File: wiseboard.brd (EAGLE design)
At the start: 80 x 55 mm, 91 parts, among them IC1 MCP73871-2CCI/ML-ND, IC2 LM358MX, Q1 IRLML6402TRPBF, Q2 IRLML6402TRPBF, U1 LT1945EMSPBF, X1 1528-1438-ND

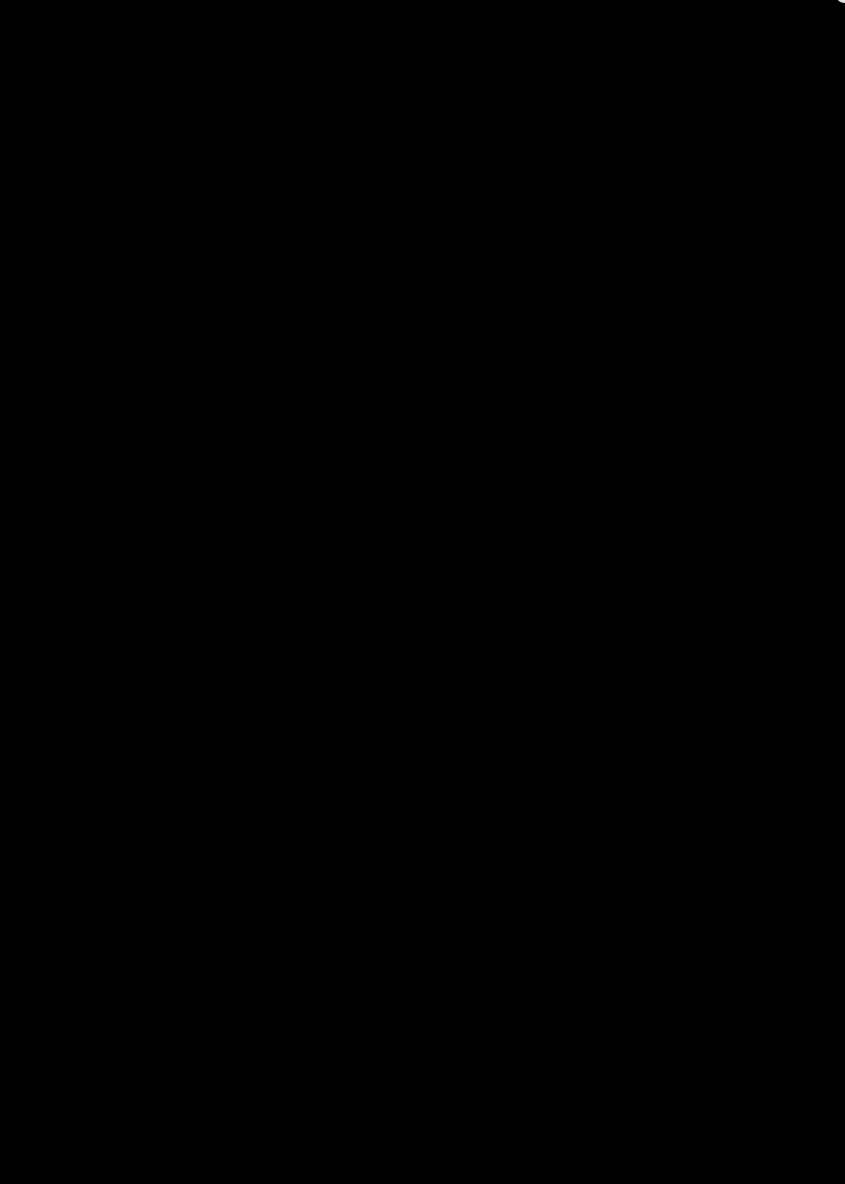
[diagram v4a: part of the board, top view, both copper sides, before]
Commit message: ADD NEW POWER SUPPLY CHIP AND UPDATED WISE LIB
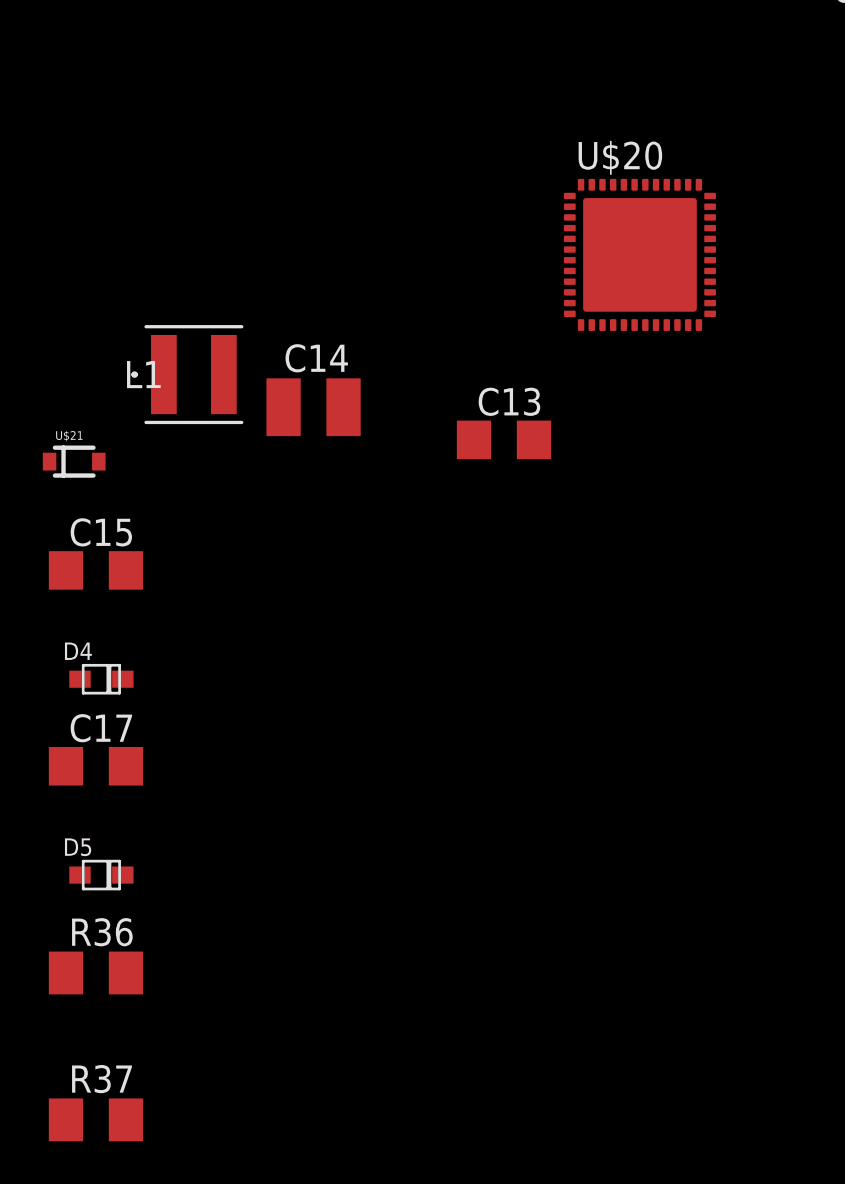
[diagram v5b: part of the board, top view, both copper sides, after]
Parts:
- added C13: 4u7F, adafruit:C1206
- added C14: 10uF, adafruit:C1210
- added C15: 100nF, adafruit:C1206
- added C17: 10nF, adafruit:C1206
- added D4, D5: (no value), adafruit:SOD-323F
- added L1: NR4012T2R2M, WISE:NR4012T2R2M
- added R36, R37: 470k, adafruit:M1206
- added U$20: TPS65186, WISE:QFN48
- added U$21: BAS3010, WISE:SOD-323
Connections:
- new net N$17: L1.2, U$20.40, U$21.2
- new net N$28: C13.2, U$20.37, U$20.42, U$21.1
- new net N$30: C15.2, D4.A, U$20.35
- new net N$32: C17.1, D4.C, D5.A
- new net N$34: C17.2, U$20.36
- new net N$36: D5.C, R36.2
- new net N$37: U$20.34
- net GND: now also C13.1, C14.1, C15.1, U$20.41
- net VBAT: now also C14.2, L1.1
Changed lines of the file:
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@@
 <element name="IC2" library="linear" library_urn="urn:adsk.eagle:library:262" package="SO08" value="LM358MX" x="33.147" y="41.148" rot="R90"/>
 <element name="CN1" library="adafruit" package="JST-PH-2-SMT-RA" value="" x="4.572" y="3.556" rot="R180"/>
+<element name="U$20" library="WISE" package="QFN48" value="TPS65186" x="7.62" y="-13.462"/>
+<element name="C13" library="adafruit" package="C1206" value="4u7F" x="1.27" y="-22.098"/>
+<element name="C14" library="adafruit" package="C1210" value="10uF" x="-7.62" y="-20.574"/>
+<element name="L1" library="WISE" package="NR4012T2R2M" value="NR4012T2R2M" x="-13.208" y="-19.05">
+<attribute name="MANUFACTURER_PART_NUMBER" value="NR4012T2R2M" x="-13.208" y="-19.05" size="1.778" layer="27" display="off"/>
+<attribute name="VENDOR" value="Taiyo Yuden" x="-13.208" y="-19.05" size="1.778" layer="27" display="off"/>
+</element>
+<element name="U$21" library="WISE" package="SOD-323" value="BAS3010" x="-18.796" y="-23.114"/>
+<element name="C15" library="adafruit" package="C1206" value="100nF" x="-17.78" y="-28.194"/>
+<element name="D4" library="adafruit" package="SOD-323F" value="" x="-17.526" y="-33.274"/>
+<element name="C17" library="adafruit" package="C1206" value="10nF" x="-17.78" y="-37.338"/>
+<element name="D5" library="adafruit" package="SOD-323F" value="" x="-17.526" y="-42.418"/>
+<element name="R36" library="adafruit" package="M1206" value="470k" x="-17.78" y="-46.99"/>
+<element name="R37" library="adafruit" package="M1206" value="470k" x="-17.78" y="-53.848"/>
 </elements>
 <signals>
@@
 <wire x1="10.506175" y1="10.5184" x2="14.8876" y2="10.5184" width="0.1524" layer="1"/>
 <wire x1="14.8876" y1="10.5184" x2="15.008" y2="10.398" width="0.1524" layer="1"/>
-<wire x1="20.574" y1="37.846" x2="22.2885" y2="36.5125" width="0" layer="19" extent="1-1"/>
+<contactref element="C13" pad="1"/>
+<contactref element="C14" pad="1"/>
+<contactref element="U$20" pad="41"/>
+<contactref element="C15" pad="1"/>
+<wire x1="57.429" y1="32.5685" x2="75.695" y2="20.32" width="0" layer="19" extent="1-1"/>
+<wire x1="55.245" y1="29.0195" x2="57.429" y2="32.5685" width="0" layer="19" extent="1-1"/>
+<wire x1="49.5935" y1="33.274" x2="55.245" y2="29.0195" width="0" layer="19" extent="1-1"/>
+<wire x1="47.6826" y1="35.2366" x2="49.5935" y2="33.274" width="0" layer="19" extent="1-1"/>
 <wire x1="43.688" y1="36.068" x2="43.5776" y2="33.6384" width="0" layer="19" extent="16-16"/>
-<wire x1="49.5935" y1="33.274" x2="47.6826" y2="35.2366" width="0" layer="19" extent="1-1"/>
+<wire x1="27.746" y1="40.513" x2="31.2308125" y2="36.0121" width="0" layer="19" extent="1-1"/>
+<wire x1="27.746" y1="41.783" x2="27.746" y2="40.513" width="0" layer="19" extent="1-1"/>
+<wire x1="22.546" y1="41.783" x2="27.746" y2="41.783" width="0" layer="19" extent="1-1"/>
+<wire x1="22.546" y1="40.513" x2="22.546" y2="41.783" width="0" layer="19" extent="1-1"/>
+<wire x1="20.574" y1="37.846" x2="22.546" y2="40.513" width="0" layer="19" extent="1-1"/>
+<wire x1="22.2885" y1="36.5125" x2="20.574" y2="37.846" width="0" layer="19" extent="1-1"/>
+<wire x1="23.3045" y1="35.7759" x2="22.2885" y2="35.7759" width="0" layer="19" extent="1-1"/>
 <wire x1="22.7965" y1="31.4071" x2="18.9808" y2="31.496" width="0" layer="19" extent="1-16"/>
 <wire x1="30.858" y1="22.479" x2="30.731" y2="25.273" width="0" layer="19" extent="1-1"/>
-<wire x1="27.746" y1="40.513" x2="22.546" y2="40.513" width="0" layer="19" extent="1-1"/>
-<wire x1="7.112" y1="43.825" x2="11.079" y2="43.942" width="0" layer="19" extent="1-1"/>
 <wire x1="30.48" y1="17.015" x2="30.858" y2="22.479" width="0" layer="19" extent="1-1"/>
 <wire x1="25.397" y1="16.256" x2="30.48" y2="17.015" width="0" layer="19" extent="1-1"/>
 <wire x1="22.733" y1="16.8025" x2="25.397" y2="16.256" width="0" layer="19" extent="1-1"/>
-<wire x1="29.0322" y1="50.7746" x2="33.3248" y2="46.2534" width="0" layer="19" extent="1-1"/>
 <wire x1="28.448" y1="10.6015" x2="25.397" y2="16.256" width="0" layer="19" extent="1-1"/>
 <wire x1="34.147" y1="10.065" x2="28.448" y2="10.6015" width="0" layer="19" extent="1-1"/>
+<wire x1="35.147" y1="11.065" x2="34.147" y2="10.065" width="0" layer="19" extent="1-1"/>
 <wire x1="37.973" y1="10.77" x2="35.147" y2="11.065" width="0" layer="19" extent="1-1"/>
 <wire x1="40.259" y1="10.77" x2="37.973" y2="10.77" width="0" layer="19" extent="1-1"/>
 <wire x1="40.259" y1="4.674" x2="40.259" y2="10.77" width="0" layer="19" extent="1-1"/>
+<wire x1="42.545" y1="4.674" x2="40.259" y2="4.674" width="0" layer="19" extent="1-1"/>
 <wire x1="39.624" y1="16.9" x2="40.259" y2="10.77" width="0" layer="19" extent="1-1"/>
 <wire x1="42.418" y1="17.015" x2="39.624" y2="16.9" width="0" layer="19" extent="1-1"/>
-<wire x1="55.245" y1="29.0195" x2="49.5935" y2="33.274" width="0" layer="19" extent="1-1"/>
+<wire x1="16.41475" y1="15.7226" x2="22.733" y2="16.8025" width="0" layer="19" extent="1-1"/>
+<wire x1="5.572" y1="7.256" x2="9.652" y2="10.414" width="0" layer="19" extent="1-16"/>
+<wire x1="14.986" y1="4.699" x2="15.008" y2="10.398" width="0" layer="19" extent="1-1"/>
+<wire x1="11.303" y1="2.159" x2="14.986" y2="4.699" width="0" layer="19" extent="1-1"/>
+<wire x1="16.002" y1="43.276" x2="19.304" y2="37.592" width="0" layer="19" extent="1-1"/>
+<wire x1="11.079" y1="43.942" x2="16.002" y2="43.276" width="0" layer="19" extent="1-1"/>
+<wire x1="11.306" y1="40.386" x2="11.079" y2="43.942" width="0" layer="19" extent="1-1"/>
+<wire x1="7.112" y1="43.825" x2="11.079" y2="43.942" width="0" layer="19" extent="1-1"/>
+<wire x1="3.2512" y1="38.811196875" x2="3.4483125" y2="37.9601" width="0" layer="19" extent="1-16"/>
+<wire x1="3.937" y1="41.81775" x2="5.588003125" y2="41.148" width="0" layer="19" extent="1-1"/>
+<wire x1="2.0645" y1="32.2255" x2="3.2512" y2="34.036" width="0" layer="19" extent="1-16"/>
+<wire x1="1.6575" y1="31.0255" x2="1.8281" y2="31.1961" width="0" layer="19" extent="1-1"/>
+<wire x1="1.6575" y1="29.2255" x2="1.6575" y2="31.0255" width="0" layer="19" extent="1-1"/>
+<wire x1="1.524" y1="41.81775" x2="3.937" y2="41.81775" width="0" layer="19" extent="1-1"/>
+<wire x1="1.6575" y1="22.6255" x2="1.6575" y2="29.2255" width="0" layer="19" extent="1-1"/>
+<wire x1="22.336" y1="7.256" x2="28.448" y2="10.6015" width="0" layer="19" extent="1-1"/>
+<wire x1="38.548" y1="43.053" x2="41.0408125" y2="36.4866" width="0" layer="19" extent="1-1"/>
+<wire x1="39.8272" y1="46.2534" x2="38.548" y2="43.053" width="0" layer="19" extent="1-1"/>
+<wire x1="43.561" y1="50.1015" x2="39.8272" y2="46.2534" width="0" layer="19" extent="1-1"/>
+<wire x1="33.3248" y1="46.2534" x2="38.548" y2="43.053" width="0" layer="19" extent="1-1"/>
+<wire x1="29.0322" y1="50.7746" x2="33.3248" y2="46.2534" width="0" layer="19" extent="1-1"/>
+<wire x1="22.5298" y1="50.7746" x2="29.0322" y2="50.7746" width="0" layer="19" extent="1-1"/>
+<wire x1="8.37" y1="-10.187" x2="11.303" y2="2.159" width="0" layer="19" extent="1-1"/>
+<wire x1="-0.13" y1="-22.098" x2="8.37" y2="-10.187" width="0" layer="19" extent="1-1"/>
+<wire x1="-9.02" y1="-20.574" x2="-0.13" y2="-22.098" width="0" layer="19" extent="1-1"/>
+<wire x1="-19.18" y1="-28.194" x2="-9.02" y2="-20.574" width="0" layer="19" extent="1-1"/>
 </signal>
 <signal name="VCC">
@@
 <via x="20.75" y="33.5" extent="1-16" drill="0.508"/>
 <via x="25.75" y="28.5" extent="1-16" drill="0.508"/>
+<contactref element="L1" pad="1"/>
+<contactref element="C14" pad="2"/>
+<wire x1="-6.22" y1="-20.574" x2="-14.608" y2="-19.05" width="0" layer="19" extent="1-1"/>
+<wire x1="5" y1="4.625" x2="-6.22" y2="-20.574" width="0" layer="19" extent="1-1"/>
 </signal>
 <signal name="OE">
@@
 </polygon>
 </signal>
+<signal name="N$17">
+<contactref element="U$20" pad="40"/>
+<contactref element="L1" pad="2"/>
+<contactref element="U$21" pad="2"/>
+<wire x1="-11.808" y1="-19.05" x2="-17.646" y2="-23.114" width="0" layer="19" extent="1-1"/>
+<wire x1="8.87" y1="-10.187" x2="-11.808" y2="-19.05" width="0" layer="19" extent="1-1"/>
+</signal>
+<signal name="N$28">
+<contactref element="U$21" pad="1"/>
+<contactref element="C13" pad="2"/>
+<contactref element="U$20" pad="42"/>
+<contactref element="U$20" pad="37"/>
+<wire x1="2.67" y1="-22.098" x2="-19.946" y2="-23.114" width="0" layer="19" extent="1-1"/>
+<wire x1="7.87" y1="-10.187" x2="2.67" y2="-22.098" width="0" layer="19" extent="1-1"/>
+<wire x1="10.37" y1="-10.187" x2="7.87" y2="-10.187" width="0" layer="19" extent="1-1"/>
+</signal>
+<signal name="N$30">
+<contactref element="U$20" pad="35"/>
+<contactref element="C15" pad="2"/>
+<contactref element="D4" pad="A"/>
+<wire x1="-16.38" y1="-28.194" x2="-18.526" y2="-33.274" width="0" layer="19" extent="1-1"/>
+<wire x1="10.895" y1="-11.212" x2="-16.38" y2="-28.194" width="0" layer="19" extent="1-1"/>
+</signal>
+<signal name="N$32">
+<contactref element="D4" pad="C"/>
+<contactref element="C17" pad="1"/>
+<contactref element="D5" pad="A"/>
+<wire x1="-19.18" y1="-37.338" x2="-18.526" y2="-42.418" width="0" layer="19" extent="1-1"/>
+<wire x1="-16.526" y1="-33.274" x2="-19.18" y2="-37.338" width="0" layer="19" extent="1-1"/>
+</signal>
+<signal name="N$34">
+<contactref element="U$20" pad="36"/>
+<contactref element="C17" pad="2"/>
+<wire x1="10.895" y1="-10.712" x2="-16.38" y2="-37.338" width="0" layer="19" extent="1-1"/>
+</signal>
+<signal name="N$36">
+<contactref element="D5" pad="C"/>
+<contactref element="R36" pad="2"/>
+<wire x1="-16.526" y1="-42.418" x2="-16.38" y2="-46.99" width="0" layer="19" extent="1-1"/>
+</signal>
+<signal name="N$37">
+<contactref element="U$20" pad="34"/>
+</signal>
 </signals>
